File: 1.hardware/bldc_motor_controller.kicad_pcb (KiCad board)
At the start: 2 copper layers, 150 x 100 mm, 212 parts, among them IC1 TLE8366E_V33, IC2 IS42S32800J-6TLI, IC3 STWD100NXWY3F, IC4 TPS7A2018PDBVR, J5 12V-24V Jack, J8 USB_C, Q10 IRFZ44NSTRLPBF, Q11 IRFZ44NSTRLPBF, Q12 IRFZ44NSTRLPBF, Q13 IRFZ44NSTRLPBF, Q8 IRFZ44NSTRLPBF, Q9 IRFZ44NSTRLPBF, SW1 reset_btn, U1 STM32H743BITx, U10 Hall_Analog_Joystick, U11 SN65HVD230, U3 W25Q128JVS, U4 LM2904AYD, U5 ESP32-C3-WROOM-02, U6 LM2931-5.0_SO8, U7 LM2904D, U8 LM2904D, U9 Hall_Analog_Joystick, X1 SMD3225-4

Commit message: 스펙 변경 12~48V 인풋 + 모스펫 구동에 필요한 전압 구현 필요
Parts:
- removed C30, C34: 0.01uF/50V, Capacitor_SMD:C_0402_1005Metric
- removed C31: 100uF/50V, Capacitor_THT:CP_Radial_Tantal_D8.0mm_P5.00mm
- removed C32, C56: 0.22uF/50V, Capacitor_SMD:C_0603_1608Metric
- removed C33, C54, C55: 0.1uF/50V, Capacitor_SMD:C_0402_1005Metric
- removed C53: 100uF/16V, Capacitor_THT:CP_Radial_Tantal_D8.0mm_P5.00mm
- removed C62: 0.1uF/16V, Capacitor_SMD:C_0402_1005Metric
- removed D14: B540C-13-F, SamacSys_Parts:DIOM7959X250N
- removed D4: Green_Led, LED_SMD:LED_0603_1608Metric
- removed D5, D6: WS2812B, LED_SMD:LED_WS2812B_PLCC4_5.0x5.0mm_P3.2mm
- removed L2: 60R_100Mhz, Inductor_SMD:L_0603_1608Metric
- removed L6: SWPA5040S3R3MT, Inductor_SMD:L_Sunlord_SWPA5040S
- removed R101, R105, R107: 4.7K/0.063w, Resistor_SMD:R_0402_1005Metric
- removed R7, R8: 0R/0.063w, Resistor_SMD:R_0402_1005Metric
- removed R9: 3.3K/0.063w, Resistor_SMD:R_0402_1005Metric
- removed SW1: reset_btn, Button_Switch_THT:SW_PUSH_6mm
- removed U4: LM2904AYD, PCM_Package_SO_AKL:SO-8_3.9x4.9mm_P1.27mm
- removed U6: LM2931-5.0_SO8, Package_SO:SOIC-8_3.9x4.9mm_P1.27mm
- removed Z1: SZ1SMB5915BT3G, SamacSys_Parts:DIOM5436X247N
- added C28: 20nF/50V, Capacitor_SMD:C_0402_1005Metric, F.Cu at (270.7, 62.8)
- added C72: 0.1uF/50V, Capacitor_SMD:C_0402_1005Metric, F.Cu at (276.4, 60.9)
- added IC5: LMR14030SDDAR, SamacSys_Parts:SOIC127P600X170-9N, F.Cu at (283.0, 49.6)
- added R138: 4.7K/0.063w, Resistor_SMD:R_0402_1005Metric, F.Cu at (232.8, 112.6)
- added R141: 10K/0.063w, Resistor_SMD:R_0402_1005Metric, F.Cu at (253.5, 39.5)
- added R142: 120/0.1w, Resistor_SMD:R_0603_1608Metric, F.Cu at (248.2, 63.3)
- added S1: TSB008A2518A, SamacSys_Parts:TSB008A2518A, F.Cu at (219.7, 67.3)
- added S2: TSB008A2518A, SamacSys_Parts:TSB008A2518A, F.Cu at (231.4, 105.2)
- added S3: TSB008A2518A, SamacSys_Parts:TSB008A2518A, F.Cu at (219.7, 72.0)
- added U15: TL431AIDBZR, SamacSys_Parts:SOT95P237X112-3N, F.Cu at (252.6, 44.6)
- C27: value 0.22uF/50V -> 0.1uF/50V; footprint Capacitor_SMD:C_0603_1608Metric -> Capacitor_SMD:C_0402_1005Metric
- C29: value 0.01uF/50V -> 0.1uF/50V
- C35: value 0.1uF/50V -> 1uF/16V
- C37: value 10uF/25V -> 1uF/16V; footprint Capacitor_SMD:C_1206_3216Metric -> Capacitor_SMD:C_0402_1005Metric
- D13: value B540C-13-F -> SS54F-HF; footprint SamacSys_Parts:DIOM7959X250N -> SamacSys_Parts:SODFL4626X120N
- D2: value SS2H10-E3_52T -> SS54F-HF; footprint SamacSys_Parts:DIOM5436X244N -> SamacSys_Parts:SODFL4626X120N
- IC1: value TLE8366E_V33 -> TPS7A2033PDBVR; footprint SamacSys_Parts:SOIC127P600X170-9N -> SamacSys_Parts:SOT95P280X145-5N
- L5: value 47uH/1.55A -> SMDRI127-6R8NT; footprint Inductor_SMD:L_SXN_SMDRI127 -> SamacSys_Parts:SMDRI1276R8NT
- LED3: value LED_0603_Red_WIFI -> LED_0603_Red
- moved IC1 253.9 mm to (287.8, 58.5)
- moved D2 242.4 mm to (282.2, 58.3)
- moved R122 240.7 mm to (253.5, 33.5)
- moved R123 240.7 mm to (253.5, 35.5)
- moved R124 240.7 mm to (253.5, 37.5)
- moved D11 236.2 mm to (247.4, 79.6)
- moved D12 236.2 mm to (247.4, 86.3)
- moved R116 234.5 mm to (250.6, 33.5)
- moved R117 234.5 mm to (250.6, 35.5)
- moved R119 234.5 mm to (250.6, 37.5)
- moved R120 234.5 mm to (250.6, 39.5)
- moved R121 234.5 mm to (250.6, 41.5)
- moved JP1 226.3 mm to (245.6, 99.2)
- moved C68 226.2 mm to (252.5, 58.9)
- moved C69 226.2 mm to (252.5, 60.9)
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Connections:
- net Net-(R127-Pad2) renamed CURRENT_U
- net Net-(R128-Pad2) renamed CURRENT_V
- net Net-(R131-Pad2) renamed CURRENT_W
- C27 pad 1: Net-(IC1-BDS) -> Net-(IC5-BOOT)
- C27 pad 2: Net-(IC1-BUO) -> Net-(IC5-SW)
- C29 pad 1: Net-(IC1-COMP) -> PWR_INPUT(12V~24V)
- C29 pad 2: Net-(C29-Pad2) -> GND
- C35 pad 1: Net-(IC1-FB) -> 3V3
- C36 pad 1: +3.3V -> 3V3
- C37 pad 1: +3.3V -> 5V
- C64 pad 1: 3V3_MCU -> 5V
- C65 pad 1: 3V3_MCU -> 5V
- D2 pad 2: Net-(Q2-D) -> Net-(D2-Pad2)
- IC1 pad 1: Net-(IC1-SYNC) -> 5V
- IC1 pad 3: Net-(IC1-COMP) -> 5V
- IC1 pad 4: Net-(IC1-FB) -> unconnected-(IC1-N/C-Pad4)
- IC1 pad 5: Net-(IC1-BDS) -> 3V3
- IC4 pad 1: 3V3_MCU -> 5V
- IC4 pad 3: 3V3_MCU -> 5V
- J5 pad 1: Net-(D14-Pad2) -> Net-(D2-Pad2)
- L1 pad 1: +3.3V -> 3V3
- L3 pad 1: +3.3V -> 3V3
- L5 pad 1: Net-(IC1-BUO) -> 5V
- L5 pad 2: Net-(IC1-FB) -> Net-(IC5-SW)
- Q10 pad 1: unconnected-(Q10-Pad1) -> Net-(Q10-Pad1)
- Q10 pad 3: unconnected-(Q10-Pad3) -> MOTOR_V
- Q11 pad 1: unconnected-(Q11-Pad1) -> Net-(Q11-Pad1)
- Q11 pad 2: unconnected-(Q11-Pad2) -> MOTOR_V
- Q12 pad 1: unconnected-(Q12-Pad1) -> Net-(Q12-Pad1)
- Q12 pad 3: unconnected-(Q12-Pad3) -> MOTOR_W
- Q13 pad 1: unconnected-(Q13-Pad1) -> Net-(Q13-Pad1)
- Q13 pad 2: unconnected-(Q13-Pad2) -> MOTOR_W
- Q8 pad 1: unconnected-(Q8-Pad1) -> Net-(Q8-Pad1)
- Q8 pad 3: unconnected-(Q8-Pad3) -> MOTOR_U
- Q9 pad 1: unconnected-(Q9-Pad1) -> Net-(Q9-Pad1)
- Q9 pad 2: unconnected-(Q9-Pad2) -> MOTOR_U
- U1 pad 145: USB_DM -> Net-(U1-PA11)
- U1 pad 146: USB_DP -> Net-(U1-PA12)
- U1 pad 197: unconnected-(U1-BOOT0-Pad197) -> Net-(U1-BOOT0)
- U1 pad 41: unconnected-(U1-VREF+-Pad41) -> ADC_VREF_2V5
- U1 pad 42: unconnected-(U1-VDDA-Pad42) -> MCU_VDD
- U1 pad 6: unconnected-(U1-VBAT-Pad6) -> MCU_VDD
- U5 pad 15: GND -> Net-(LED3-K)
- U5 pad 2: Net-(U5-EN) -> ESP_EN
- U5 pad 8: Net-(LED3-K) -> ESP_BOOT
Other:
- board size 150 x 100 mm -> 150 x 150 mm

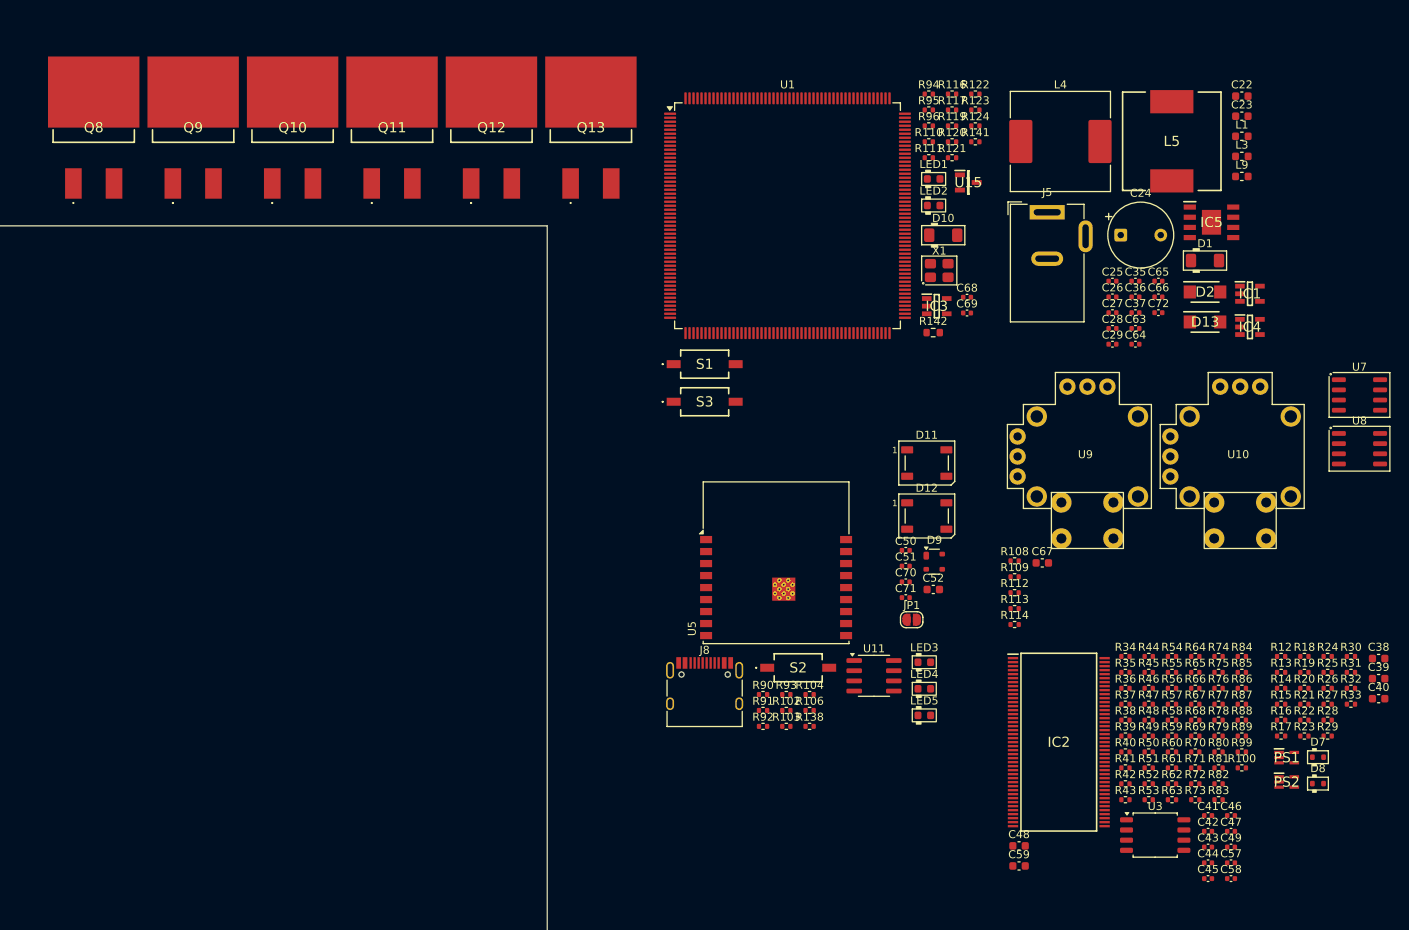
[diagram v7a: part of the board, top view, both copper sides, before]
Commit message: mosfet 확정 및 드라이버 고려중 자세한 계산식 필요
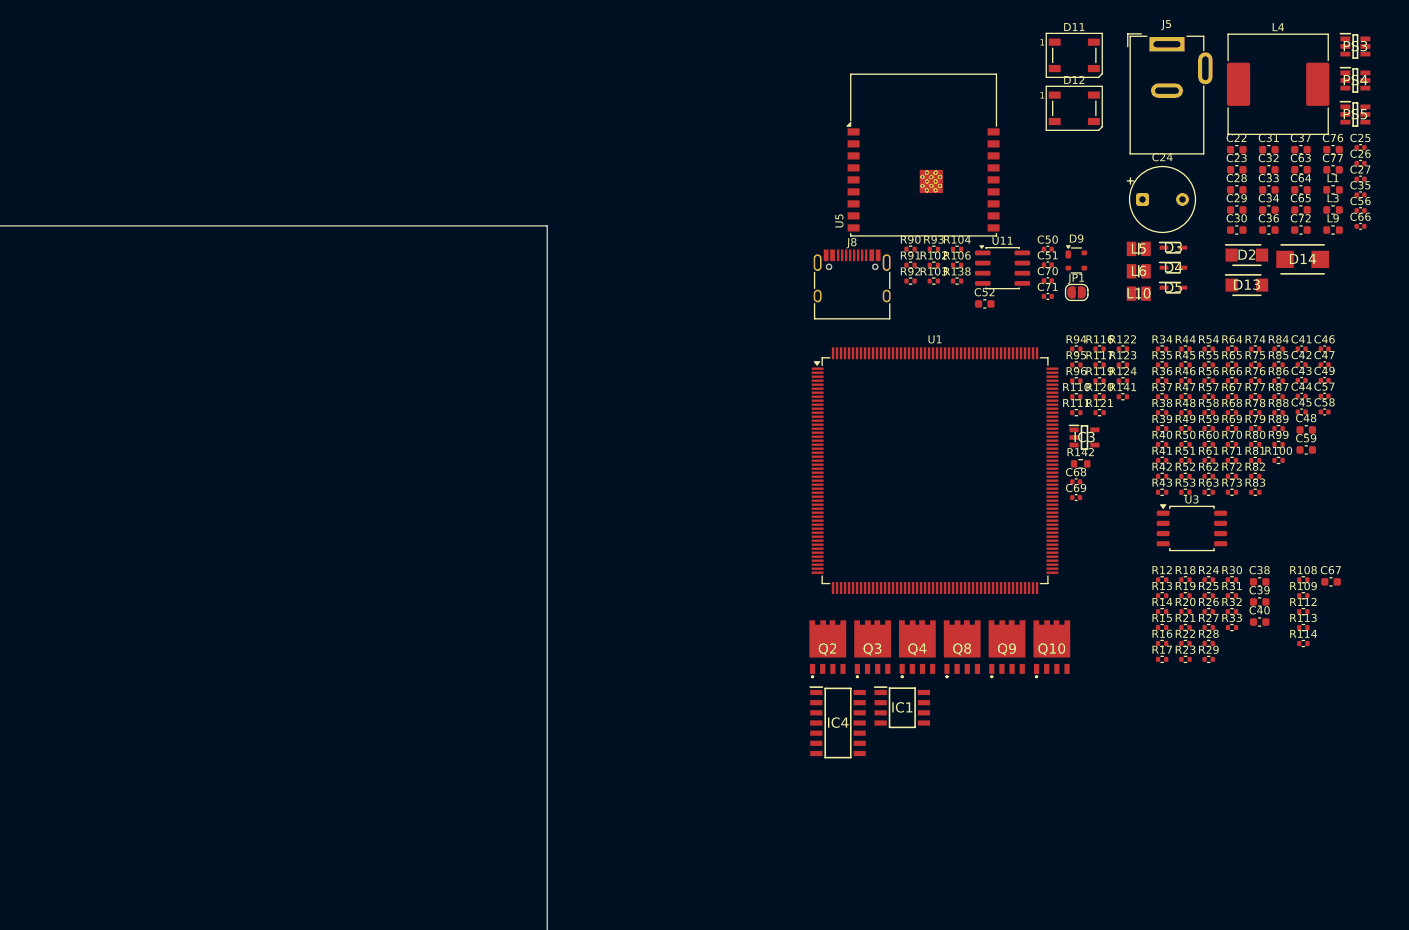
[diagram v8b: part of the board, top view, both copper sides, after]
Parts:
- removed D1, D10: LL4148, PCM_Diode_SMD_AKL:D_MiniMELF
- removed D7, D8: NSR0240V2, PCM_Diode_SMD_AKL:D_SOD-523
- removed IC2: IS42S32800J-6TLI, SamacSys_Parts:SOP50P1176X120-86N
- removed IC5: LMR14030SDDAR, SamacSys_Parts:SOIC127P600X170-9N
- removed LED1, LED2: LED_0603_Blue, PCM_LED_SMD_AKL:LED_0603_1608Metric
- removed LED3: LED_0603_Red, PCM_LED_SMD_AKL:LED_0603_1608Metric
- removed LED4: LED_0603_Blue_BLE, PCM_LED_SMD_AKL:LED_0603_1608Metric
- removed LED5: LED_0603_Green_PWR, PCM_LED_SMD_AKL:LED_0603_1608Metric
- removed PS1, PS2: TPS61169DCKR, SamacSys_Parts:SOT65P210X110-5N
- removed Q11, Q12, Q13: IRFZ44NSTRLPBF, SamacSys_Parts:IRFZ44NSTRLPBF
- removed S1, S2, S3: TSB008A2518A, SamacSys_Parts:TSB008A2518A
- removed U10, U9: Hall_Analog_Joystick, New_Footprints:Hall_Analog_Joystick
- removed U15: TL431AIDBZR, SamacSys_Parts:SOT95P237X112-3N
- removed U7, U8: LM2904D, PCM_Package_SO_AKL:SO-8_3.9x4.9mm_P1.27mm
- removed X1: SMD3225-4, PCM_Crystal_AKL:Crystal_SMD_3225-4Pin_3.2x2.5mm
- added C30: 10uF/25V, Capacitor_SMD:C_0603_1608Metric, F.Cu at (286.2, 50.5)
- added C31: 10uF/25V, Capacitor_SMD:C_0603_1608Metric, F.Cu at (290.2, 40.5)
- added C32: 0.1uF/50V, Capacitor_SMD:C_0603_1608Metric, F.Cu at (290.2, 43.0)
- added C33: 22uF/10V, Capacitor_SMD:C_0603_1608Metric, F.Cu at (290.2, 45.5)
- added C34: 22uF/10V, Capacitor_SMD:C_0603_1608Metric, F.Cu at (290.2, 48.0)
- added C56: 0.1uF/50V, Capacitor_SMD:C_0402_1005Metric, F.Cu at (301.7, 48.1)
- added C76: 10uF/25V, Capacitor_SMD:C_0603_1608Metric, F.Cu at (298.2, 40.5)
- added C77: 0.1uF/50V, Capacitor_SMD:C_0603_1608Metric, F.Cu at (298.2, 43.0)
- added D14: SMBJ28CA-Q, SamacSys_Parts:DIONM5436X244N, F.Cu at (294.4, 54.2)
- added D3: B5819WS, SamacSys_Parts:SOD2613X100N, F.Cu at (278.3, 52.7)
- added D4: B5819WS, SamacSys_Parts:SOD2613X100N, F.Cu at (278.3, 55.2)
- added D5: B5819WS, SamacSys_Parts:SOD2613X100N, F.Cu at (278.3, 57.7)
- added L10: MPL2016S3R3MHT, SamacSys_Parts:INDC2116X100N, F.Cu at (273.9, 58.5)
- added L6: MPL2016S2R2MHT, SamacSys_Parts:INDC2116X100N, F.Cu at (273.9, 55.7)
- added PS3: TPS563201DDCT, SamacSys_Parts:SOT95P280X110-6N, F.Cu at (301.0, 27.6)
- added PS4: TPS563201DDCT, SamacSys_Parts:SOT95P280X110-6N, F.Cu at (301.0, 31.8)
- added PS5: TPS563201DDCT, SamacSys_Parts:SOT95P280X110-6N, F.Cu at (301.0, 36.1)
- added Q2: STL130N6F7, SamacSys_Parts:FERD20U50DJFTR, F.Cu at (235.2, 105.5)
- added Q3: STL130N6F7, SamacSys_Parts:FERD20U50DJFTR, F.Cu at (240.8, 105.5)
- added Q4: STL130N6F7, SamacSys_Parts:FERD20U50DJFTR, F.Cu at (246.4, 105.5)
- C23: value 0.22uF/50V -> 0.22uF/100V
- C24: value 100uF/50V -> 100uF/100V
- C25: value 0.1uF/50V -> 0.1uF/100V
- C26: value 0.01uF/50V -> 0.01uF/100V
- C28: value 20nF/50V -> 22uF/10V; footprint Capacitor_SMD:C_0402_1005Metric -> Capacitor_SMD:C_0603_1608Metric
- C29, C64: value 0.1uF/50V -> 22uF/10V; footprint Capacitor_SMD:C_0402_1005Metric -> Capacitor_SMD:C_0603_1608Metric
- C35, C66: value 1uF/16V -> 0.1uF/50V
- C36, C72: value 0.1uF/50V -> 10uF/25V; footprint Capacitor_SMD:C_0402_1005Metric -> Capacitor_SMD:C_0603_1608Metric
- C37: value 1uF/16V -> 10uF/25V; footprint Capacitor_SMD:C_0402_1005Metric -> Capacitor_SMD:C_0603_1608Metric
- C63: footprint Capacitor_SMD:C_0402_1005Metric -> Capacitor_SMD:C_0603_1608Metric
- C65: value 1uF/16V -> 22uF/10V; footprint Capacitor_SMD:C_0402_1005Metric -> Capacitor_SMD:C_0603_1608Metric
- IC1: value TPS7A2033PDBVR -> UCC27712QDRQ1; footprint SamacSys_Parts:SOT95P280X145-5N -> SamacSys_Parts:SOIC127P600X175-8N
- IC4: value TPS7A2018PDBVR -> SN74HC266D; footprint SamacSys_Parts:SOT95P280X145-5N -> SamacSys_Parts:SOIC127P600X175-14N
- J5: value 12V-24V Jack -> 12V-48V Jack
- L4: value 47uH/1.55A -> SMMS1050-470M
- L5: value SMDRI127-6R8NT -> MPL2016S2R2MHT; footprint SamacSys_Parts:SMDRI1276R8NT -> SamacSys_Parts:INDC2116X100N
- Q10, Q8, Q9: value IRFZ44NSTRLPBF -> STL130N6F7; footprint SamacSys_Parts:IRFZ44NSTRLPBF -> SamacSys_Parts:FERD20U50DJFTR
- moved Q8 128.1 mm to (252.0, 105.5)
- moved Q9 122.4 mm to (257.6, 105.5)
- moved Q10 116.8 mm to (263.2, 105.5)
- moved IC4 71.4 mm to (236.3, 112.1)
- moved IC1 67.6 mm to (244.4, 110.2)
- moved C48 63.2 mm to (294.9, 75.5)
- moved C59 63.2 mm to (294.9, 78.0)
- moved C42 59.5 mm to (294.3, 67.3)
- moved C43 59.5 mm to (294.3, 69.3)
- moved C47 59.5 mm to (297.2, 67.3)
- moved C49 59.5 mm to (297.2, 69.3)
- moved C41 59.5 mm to (294.3, 65.4)
- moved C44 59.5 mm to (294.3, 71.3)
- moved C45 59.5 mm to (294.3, 73.3)
- moved C46 59.5 mm to (297.2, 65.4)
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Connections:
- net PWR_INPUT(5V~24V) renamed PWR_INPUT(12V~48V)
- C27 pad 1: Net-(IC5-BOOT) -> Net-(PS5-SW)
- C27 pad 2: Net-(IC5-SW) -> Net-(PS5-VBST)
- C28 pad 1: Net-(IC5-SS) -> 1V8
- C29 pad 1: PWR_INPUT(12V~24V) -> 1V8
- C35 pad 1: 3V3 -> Net-(PS3-SW)
- C35 pad 2: GND -> Net-(PS3-VBST)
- C36 pad 1: 3V3 -> Net-(PS3-VIN)
- C37 pad 1: 5V -> Net-(PS3-VIN)
- C63 pad 1: 1V8 -> Net-(PS3-VIN)
- C66 pad 1: 1V8 -> Net-(PS4-SW)
- C66 pad 2: GND -> Net-(PS4-VBST)
- C72 pad 1: 5V -> Net-(PS4-VIN)
- IC1 pad 1: 5V -> unconnected-(IC1-LI-Pad1)
- IC1 pad 2: GND -> unconnected-(IC1-HI-Pad2)
- IC1 pad 3: 5V -> unconnected-(IC1-VDD-Pad3)
- IC1 pad 5: 3V3 -> unconnected-(IC1-LO-Pad5)
- IC4 pad 1: 5V -> unconnected-(IC4-1A-Pad1)
- IC4 pad 2: GND -> unconnected-(IC4-1B-Pad2)
- IC4 pad 3: 5V -> unconnected-(IC4-1Y-Pad3)
- IC4 pad 5: 1V8 -> unconnected-(IC4-2A-Pad5)
- L5 pad 1: 5V -> 1V8
- L5 pad 2: Net-(IC5-SW) -> Net-(PS5-SW)
- Q10 pad 1: Net-(Q10-Pad1) -> unconnected-(Q10-S_1-Pad1)
- Q10 pad 3: MOTOR_V -> unconnected-(Q10-S_3-Pad3)
- Q8 pad 1: Net-(Q8-Pad1) -> unconnected-(Q8-S_1-Pad1)
- Q8 pad 3: MOTOR_U -> unconnected-(Q8-S_3-Pad3)
- Q9 pad 1: Net-(Q9-Pad1) -> unconnected-(Q9-S_1-Pad1)
- Q9 pad 2: MOTOR_U -> unconnected-(Q9-S_2-Pad2)
- Q9 pad 3: Net-(Q9-Pad3) -> unconnected-(Q9-S_3-Pad3)
